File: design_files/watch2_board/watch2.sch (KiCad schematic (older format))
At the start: 46 parts, among them J1 USB_C_Receptacle_USB2.0, J2 STEMMA QT, J3 Conn_01x03_Male, J4 Conn_01x03_Male, J5 TFT Connector, Q1 Q_NPN_BCE, SW1 SW_Push, SW2 SW_Push, U1 FT230XS, U2 MCP73831-2-OT, U3 MAX17043G+U, U4 MAX16150AUT+T, U5 MAX604, U6 MCP23008-xSO, U7 ESP32-WROVER, U8 MAX98357AETE+T

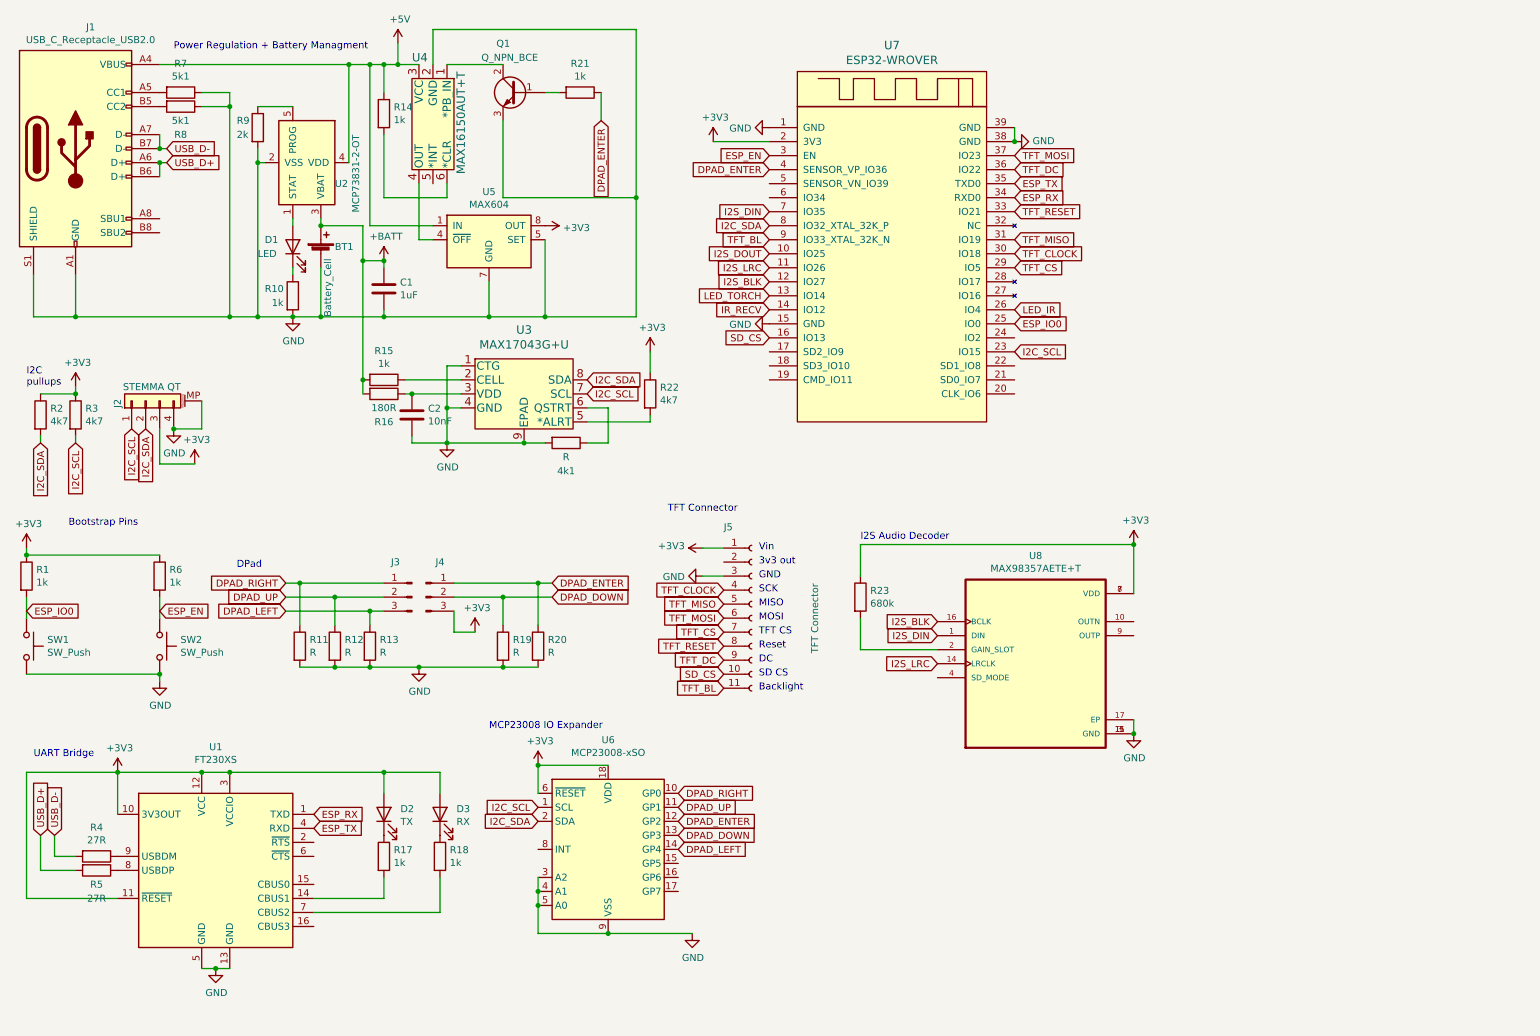
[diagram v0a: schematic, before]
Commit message: added torch + ir stuff to schematic and did some pcb stuff
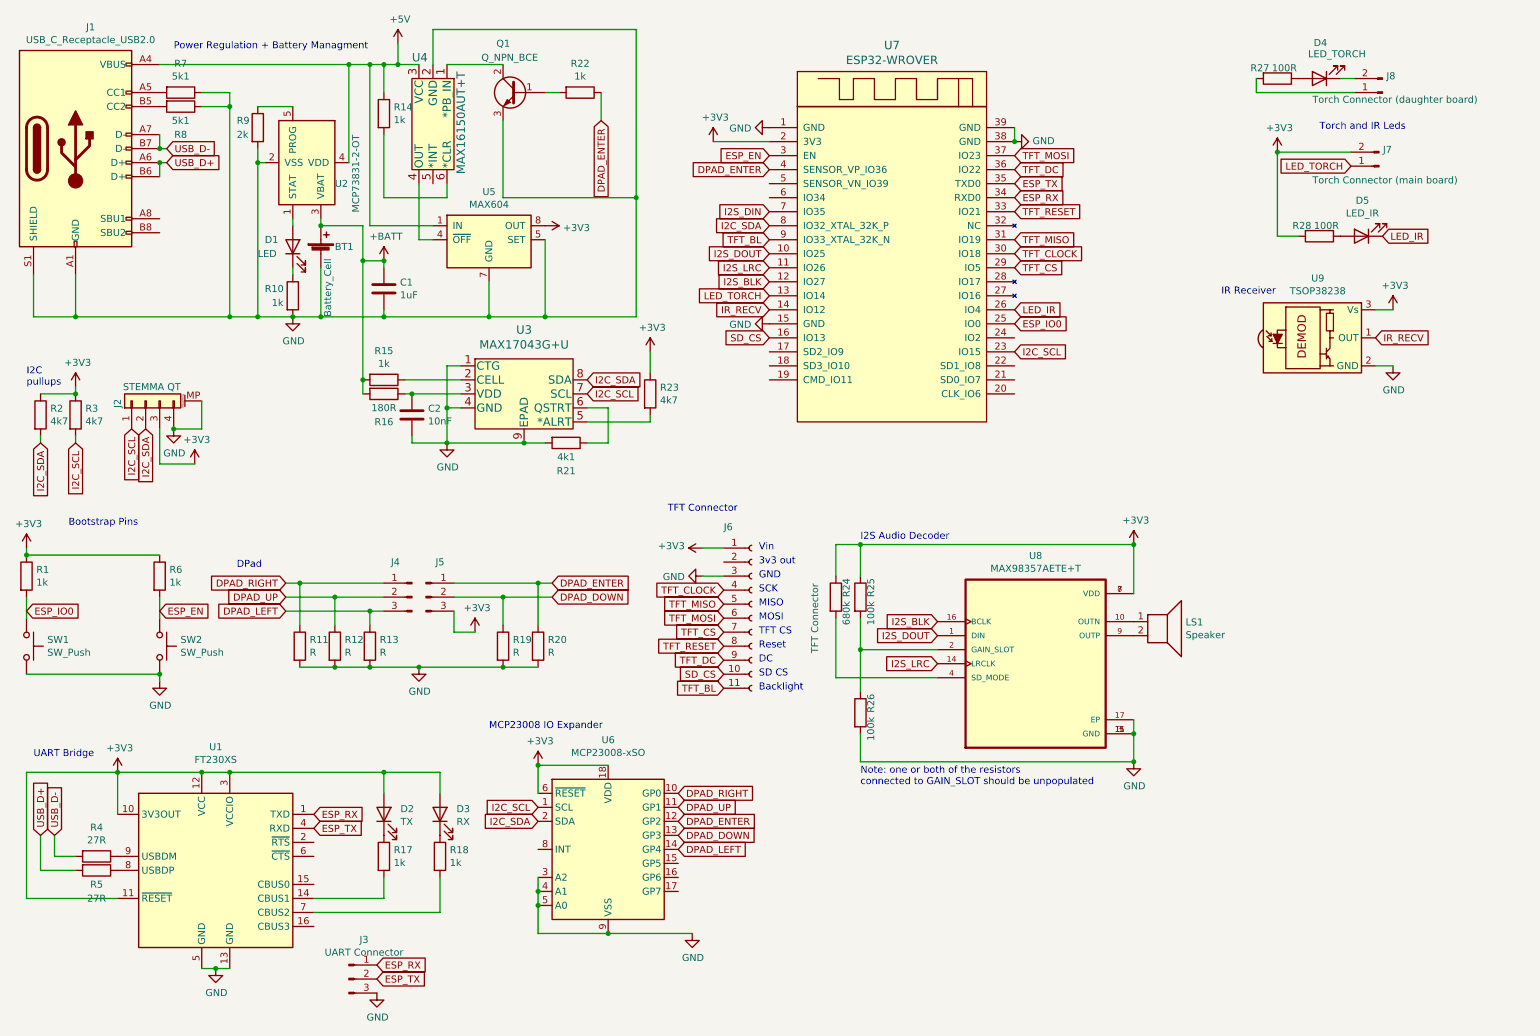
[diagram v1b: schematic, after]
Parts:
- added D4: LED_TORCH, symbol Device:LED
- added D5: LED_IR, symbol Device:LED
- added J3: UART Connector, symbol Connector:Conn_01x03_Male
- added J7: Torch Connector (main board), symbol Connector:Conn_01x02_Male
- added J8: Torch Connector (daughter board), symbol Connector:Conn_01x02_Male
- added LS1: Speaker, symbol Device:Speaker
- added R25, R26: 100k, symbol Device:R
- added R27, R28: 100R, symbol Device:R
- added U9: TSOP38238, OptoDevice:Vishay_MINICAST-3Pin, symbol Interface_Optical:TSOP382xx
- R21: renamed from 4k1; value R -> 4k1
- renumbered J3 to J4, J4 to J5, J5 to J6, R21 to R22, R22 to R23, R23 to R24
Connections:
- net +3V3: now also J7.2 (Pin_2), R25.1, R28.2, U9.3 (Vs)
- net ESP_RX: now also J3.1 (Pin_1)
- net ESP_TX: now also J3.2 (Pin_2)
- net GND: now also J3.3 (Pin_3), R26.2, U9.2 (GND)
- net I2S_DIN: no longer U8.1 (DIN)
- net I2S_DOUT: now also U8.1 (DIN)
- net IR_RECV: now also U9.1 (OUT)
- net LED_IR: now also D5.1 (K)
- net LED_TORCH: now also J7.1 (Pin_1)
- net at U8.10 (OUTN): now also LS1.1
- net at U8.2 (GAIN_SLOT): now also R25.2, R26.1; no longer R24.2
- net at U8.4 (SD_MODE): now also R24.2
- net at U8.9 (OUTP): now also LS1.2
- new net: D4.1 (K), J8.2 (Pin_2)
- new net: D4.2 (A), R27.1
- new net: J8.1 (Pin_1), R27.2
- new net: D5.2 (A), R28.1
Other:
- note added: "IR Receiver"
- note added: "Note: one or both of the resistors \nconnected to GAIN_SLOT should be unpopulated"
- note added: "Torch and IR Leds"
- moved on the sheet: R24

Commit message: added transistors to leds in schematic
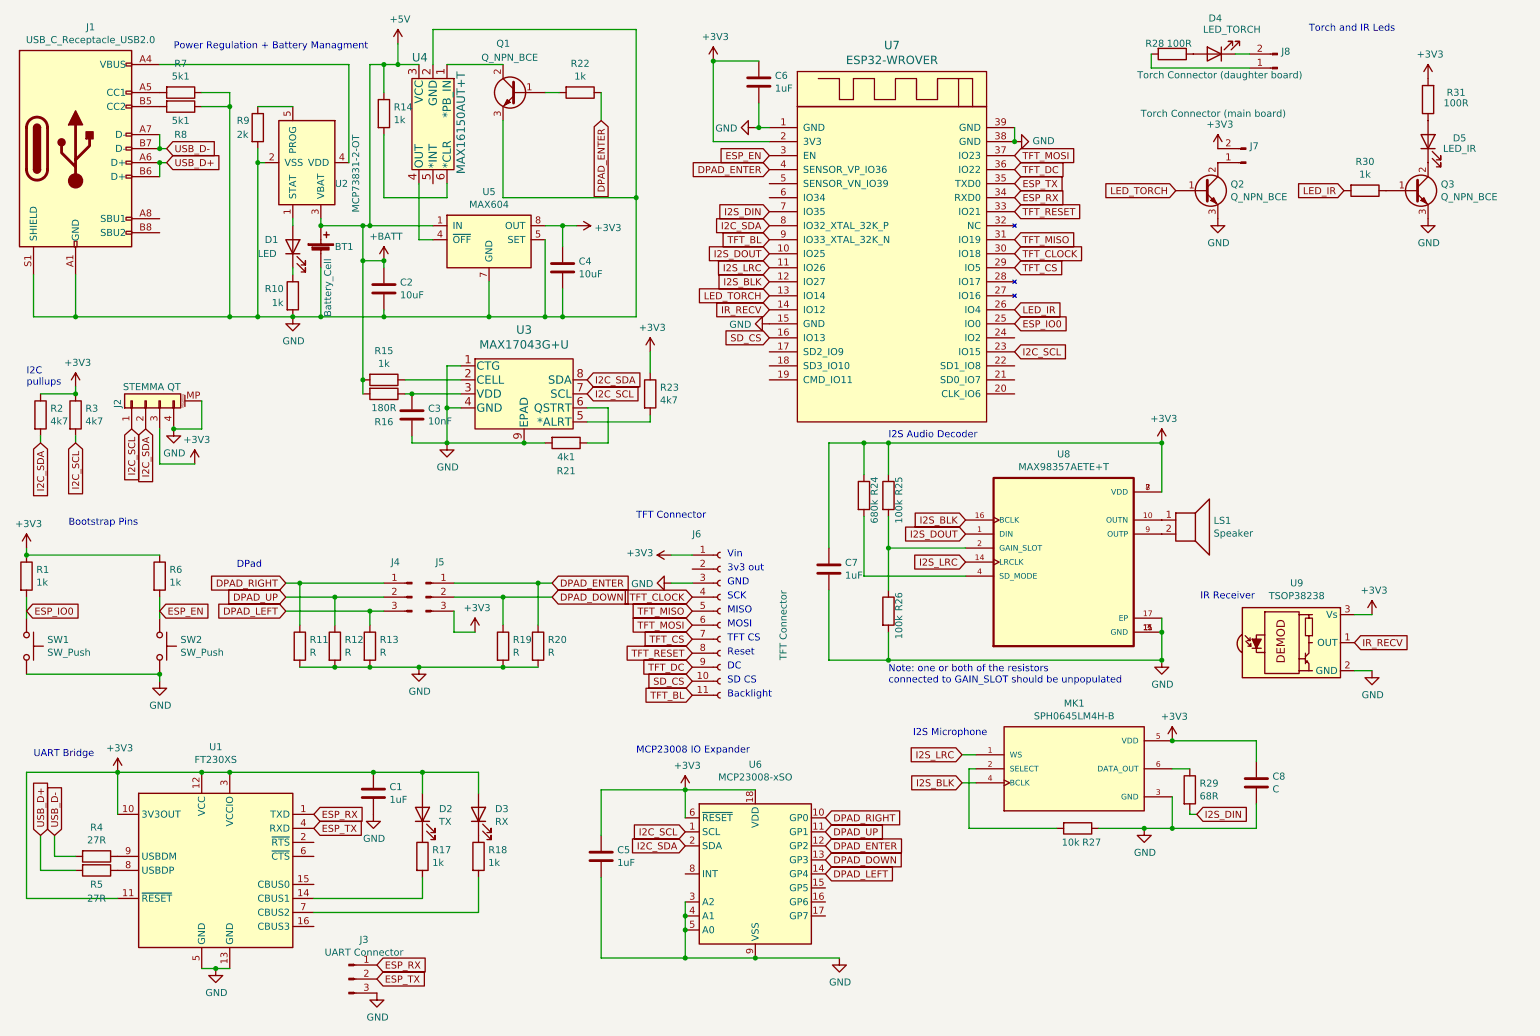
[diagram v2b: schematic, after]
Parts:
- added C1, C5, C6, C7: 1uF, symbol Device:C
- added C4: 10uF, symbol Device:C
- added C8: C, symbol Device:C
- added MK1: SPH0645LM4H-B, MIC_SPH0645LM4H-B, symbol SPH0645LM4H-B:SPH0645LM4H-B
- added Q2, Q3: Q_NPN_BCE, symbol Device:Q_NPN_BCE
- added R27: 10k, symbol Device:R
- added R29: 68R, symbol Device:R
- added R30: 1k, symbol Device:R
- C2: renamed from C1; value 1uF -> 10uF
- renumbered C2 to C3, R27 to R28, R28 to R31
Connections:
- net +BATT is gone; now on net +5V: BT1.1 (+), C2.1, R15.2, R16.2, U2.3 (VBAT)
- net +3V3: now also C1.1, C4.1, C5.1, C6.1, C7.1, C8.1, MK1.5 (VDD)
- net +5V: no longer J1.A4 (VBUS), J1.A9 (VBUS), J1.B4 (VBUS), J1.B9 (VBUS), U2.4 (VDD)
- net GND: now also C1.2, C4.2, C5.2, C6.2, C7.2, C8.2, MK1.3 (GND), Q2.3 (E), Q3.3 (E), R27.1
- net I2S_BLK: now also MK1.4 (BCLK)
- net I2S_DIN: now also R29.2
- net I2S_LRC: now also MK1.1 (WS)
- net LED_IR: now also R30.2; no longer D5.1 (K)
- net LED_TORCH: now also Q2.1 (B); no longer J7.1 (Pin_1)
- new net: J1.A4 (VBUS), J1.A9 (VBUS), J1.B4 (VBUS), J1.B9 (VBUS), U2.4 (VDD)
- new net: D5.1 (K), Q3.2 (C)
- new net: MK1.2 (SELECT), R27.2
- new net: MK1.6 (DATA_OUT), R29.1
- new net: Q3.1 (B), R30.1
- new net: J7.1 (Pin_1), Q2.2 (C)
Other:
- note added: "I2S Microphone"
- moved on the sheet: D2, D3, D4, D5, J6, J8, LS1, R17, R18, R24, R25, R26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

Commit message: created watch2 pcb it's mostly populated and wired up.  i haven't checked it yet, and i haven't figured out how to make IO0 externaly pressable yet :)
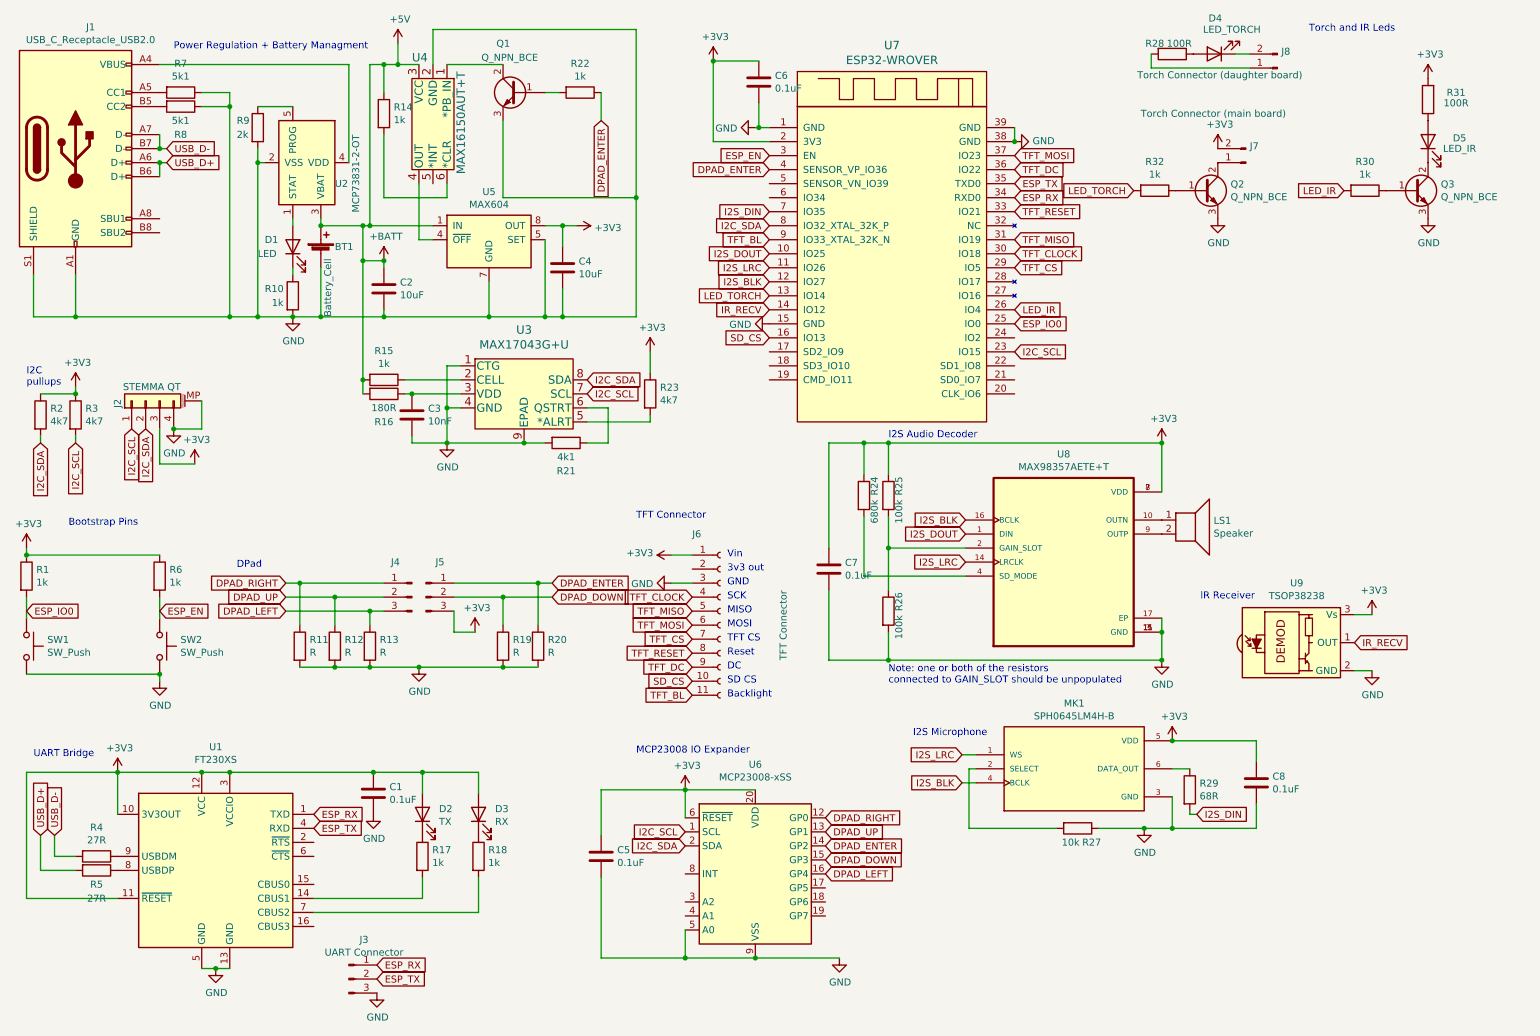
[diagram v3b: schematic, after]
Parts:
- removed U6: MCP23008-xSO, Package_SO:SOIC-18W_7.5x11.6mm_P1.27mm, symbol Interface_Expansion:MCP23008-xSO
- added R32: 1k, Resistor_SMD:R_0805_2012Metric, symbol Device:R
- added U6: MCP23008-xSS, Package_SO:SSOP-20_5.3x7.2mm_P0.65mm, symbol Interface_Expansion:MCP23008-xSS
- BT1: footprint (none) -> Connector_PinHeader_2.00mm:PinHeader_1x02_P2.00mm_Vertical
- C1, C5, C6, C7: value 1uF -> 0.1uF; footprint (none) -> Capacitor_SMD:C_0805_2012Metric
- C2, C3, C4: footprint (none) -> Capacitor_SMD:C_0805_2012Metric
- C8: value C -> 0.1uF; footprint (none) -> Capacitor_SMD:C_0805_2012Metric
- D1, D2, D3: footprint (none) -> LED_SMD:LED_0805_2012Metric_Castellated
- D4: footprint (none) -> Alice's Library:MLCAWT-A1-0000-000XE1
- D5: footprint (none) -> Alice's Library:SOD4223X290N
- J1: footprint (none) -> Alice's Library:JAE_DX07S016JA1R1500
- J2: footprint (none) -> Connector_JST:JST_SH_SM04B-SRSS-TB_1x04-1MP_P1.00mm_Horizontal
- J3: footprint (none) -> Connector_PinHeader_1.27mm:PinHeader_1x03_P1.27mm_Vertical
- J4, J5: footprint (none) -> Connector_PinHeader_2.54mm:PinHeader_1x03_P2.54mm_Vertical
- J6: footprint (none) -> Connector_PinHeader_2.54mm:PinHeader_1x11_P2.54mm_Vertical
- J7, J8: footprint (none) -> Connector_PinHeader_2.54mm:PinHeader_1x02_P2.54mm_Vertical
- LS1: footprint (none) -> Alice's Library:XDCR_CMT-7525-80-SMT-TR
- MK1: footprint MIC_SPH0645LM4H-B -> Alice's Library:MIC_SPH0645LM4H-B
- Q1, Q2, Q3: footprint (none) -> Package_TO_SOT_SMD:SOT-23
- R1, R10, R11, R12, R13, R14, R15, R16, R17, R18, R19, R2, R20, R21, R22, R23, R24, R25, R26, R27, R29, R3, R30, R4, R5, R6, R7, R8, R9: footprint (none) -> Resistor_SMD:R_0805_2012Metric
- R28, R31: footprint (none) -> Resistor_SMD:R_1812_4532Metric
- SW1, SW2: footprint (none) -> Button_Switch_SMD:SW_SPST_EVQP2
- U3: footprint 21-0174B_MXM -> Package_DFN_QFN:DFN-8-1EP_3x2mm_P0.5mm_EP1.7x1.4mm
- U4: footprint 21-0058I_MXM -> Package_TO_SOT_SMD:SOT-23-6
- U5: footprint (none) -> Package_SO:SOIC-8-1EP_3.9x4.9mm_P1.27mm_EP2.29x3mm
- U7: footprint (none) -> Alice's Library:ESP32-WROVER
- U8: footprint QFN50P300X300X80-17N -> Package_DFN_QFN:QFN-16-1EP_3x3mm_P0.5mm_EP1.7x1.7mm
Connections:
- net +3V3: now also U6.20 (VDD), U6.6 (~RESET)
- net DPAD_DOWN: now also U6.15 (GP3)
- net DPAD_ENTER: now also U6.14 (GP2)
- net DPAD_LEFT: now also U6.16 (GP4)
- net DPAD_RIGHT: now also U6.12 (GP0)
- net DPAD_UP: now also U6.13 (GP1)
- net GND: now also U6.5 (A0), U6.9 (VSS)
- net I2C_SCL: now also U6.1 (SCL)
- net I2C_SDA: now also U6.2 (SDA)
- net LED_TORCH: now also R32.2; no longer Q2.1 (B)
- new net: Q2.1 (B), R32.1

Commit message: added pcb v2 files again
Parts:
- removed Q1: Q_NPN_BCE, Package_TO_SOT_SMD:SOT-23, symbol Device:Q_NPN_BCE
- removed R16: 180R, Resistor_SMD:R_0805_2012Metric, symbol Device:R
- removed R21: 4k1, Resistor_SMD:R_0805_2012Metric, symbol Device:R
- removed R22: 1k, Resistor_SMD:R_0805_2012Metric, symbol Device:R
- removed R23: 4k7, Resistor_SMD:R_0805_2012Metric, symbol Device:R
- removed U3: MAX17043G+U, Package_DFN_QFN:DFN-8-1EP_3x2mm_P0.5mm_EP1.7x1.4mm, symbol MAX17043:MAX17043G+U
- added C9: 0.1uF, Capacitor_SMD:C_0805_2012Metric, symbol Device:C
- added SW3: Power Button, Button_Switch_SMD:SW_SPST_EVQP2, symbol Switch:SW_Push
- added U10: MCP9808_MSOP, Package_SO:MSOP-8_3x3mm_P0.65mm, symbol Sensor_Temperature:MCP9808_MSOP
- added U3: LC709203FQH-01TWG, Package_DFN_QFN:WDFN-8-1EP_4x3mm_P0.65mm_EP2.4x1.8mm, symbol Battery_Management:LC709203FQH-01TWG
- C3: value 10nF -> 0.1uF
- MK1: symbol SPH0645LM4H-B:SPH0645LM4H-B -> watch2-rescue:SPH0645LM4H-B-SPH0645LM4H-B
- Q2, Q3: symbol Device:Q_NPN_BCE -> Device:Q_NPN_BEC
- R15: value 1k -> 10k
- R28, R31: footprint Resistor_SMD:R_1812_4532Metric -> Resistor_SMD:R_1210_3225Metric
- R30, R32: value 1k -> 330R
- U4: symbol MAX16150:MAX16150AUT+T -> watch2-rescue:MAX16150AUT+T-MAX16150
- U7: symbol esp32-wrover:ESP32-WROVER -> watch2-rescue:ESP32-WROVER-esp32-wrover
- U8: symbol MAX98357AETE_T:MAX98357AETE+T -> watch2-rescue:MAX98357AETE+T-MAX98357AETE_T
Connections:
- net +3V3: now also J2.2 (Pin_2), C9.1, U10.8 (VDD); no longer J2.3 (Pin_3)
- net +5V: now also C3.1, R15.1, U3.3 (VDD); no longer R15.2
- net GND: now also J2.1 (Pin_1), Q2.2 (E), Q3.2 (E), U6.3 (A2), U6.4 (A1), C9.2, SW3.2, U10.4 (GND), U10.5 (A2), U10.6 (A1), U10.7 (A0), U3.1 (TEST), U3.2 (VSS), U3.9 (EP); no longer J2.4 (Pin_4), Q2.3 (E), Q3.3 (E), R10.2
- net I2C_SCL: now also J2.4 (Pin_4), U10.2 (SCL), U3.8 (SCL); no longer J2.1 (Pin_1)
- net I2C_SDA: now also J2.3 (Pin_3), U10.1 (SDA), U3.7 (SDA); no longer J2.2 (Pin_2)
- net at U2.1 (STAT): now also D1.1 (K); no longer D1.2 (A)
- net at J1.A4 (VBUS), J1.A9 (VBUS), J1.B4 (VBUS)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: now also R10.2
- net at R10.1: now also D1.2 (A); no longer D1.1 (K)
- net at D4.2 (A): now also J8.1 (Pin_1); no longer R28.1
- net at R28.2: now also Q2.3 (C); no longer J8.1 (Pin_1)
- net at D5.1 (K): now also Q3.3 (C); no longer Q3.2 (C)
- net at U4.1 (*PB_IN): now also SW3.1
- net at J7.1 (Pin_1): now also R28.1; no longer Q2.2 (C)
- new net: R15.2, U3.4 (~ALARMB)
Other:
- moved on the sheet: D1, J7, R10, R28
